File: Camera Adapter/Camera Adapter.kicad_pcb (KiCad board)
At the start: 2 copper layers, 30 x 50 mm, 13 parts, among them J1 Conn_02x15_Top_Bottom, J2 634108150321, J3 Conn_01x02, J4 Conn_01x03, J5 Conn_02x15_Top_Bottom, J6 634108150321, U1 MC33269D-3.3G

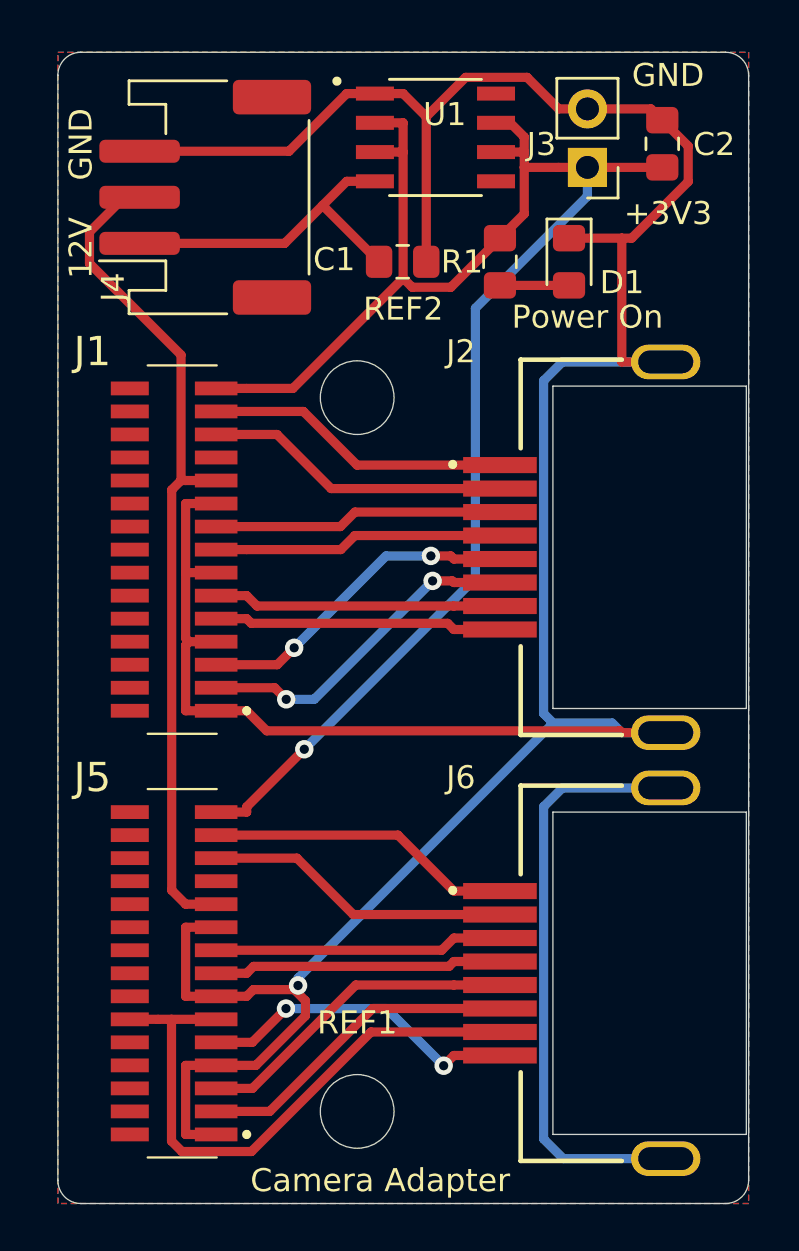
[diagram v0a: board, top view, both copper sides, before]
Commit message: Change to different ZIF connector
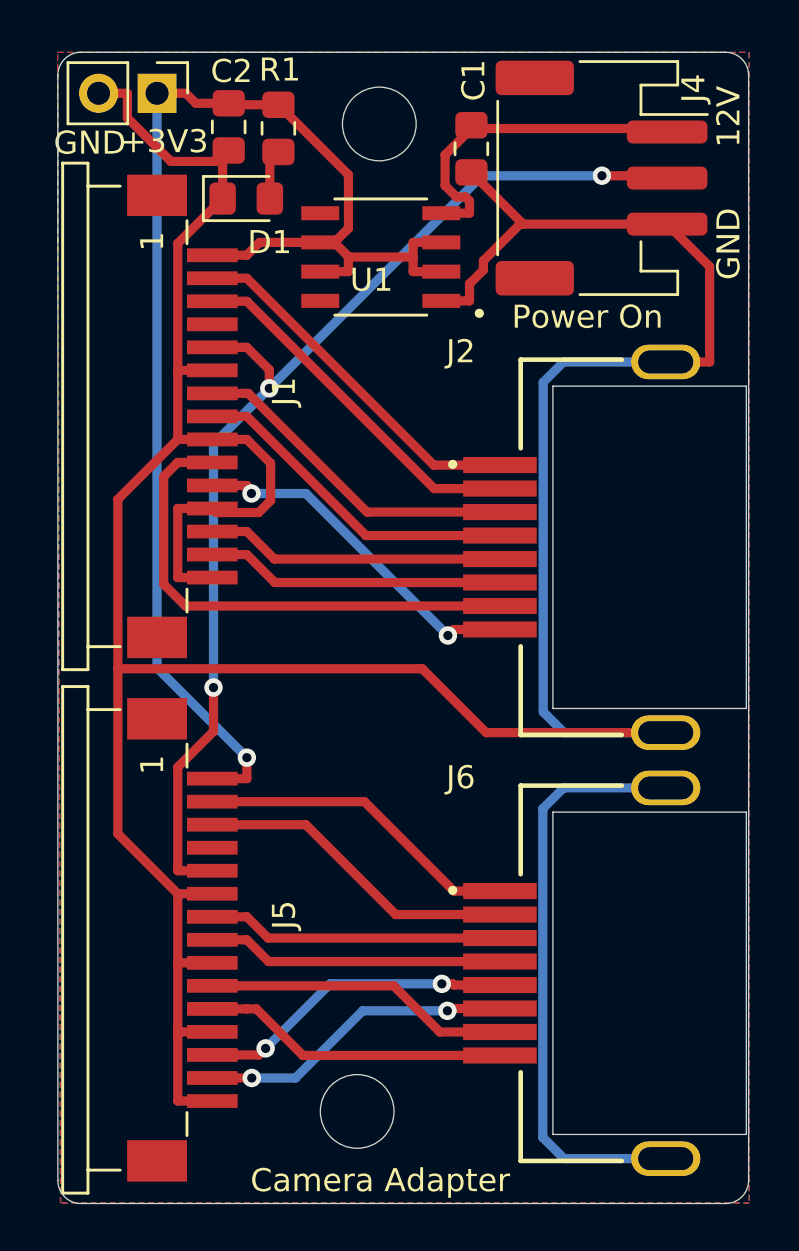
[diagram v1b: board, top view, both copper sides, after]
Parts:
- J1, J5: value Conn_02x15_Top_Bottom -> 68611514122; footprint digikey-footprints:117342485 -> digikey-footprints:68611514122
- moved J3 19.0 mm to (51.3, 29.8), turned to 270 degrees
- moved C2 18.8 mm to (54.4, 31.2), turned to 270 degrees
- moved J4 17.2 mm to (70.6, 33.5), turned to 270 degrees
- moved D1 14.3 mm to (55.2, 34.4), turned to 0 degrees
- moved REF2 11.9 mm to (61.0, 31.1)
- moved R1 11.2 mm to (56.6, 31.3)
- moved J1 6.34 mm to (51.3, 43.8)
- moved C1 5.74 mm to (65.0, 32.2), turned to 270 degrees
- moved U1 5.71 mm to (61.0, 36.9), turned to 180 degrees
- moved J5 2.97 mm to (51.3, 66.5)
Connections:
- J1 pad 1: GND -> +3V3
- J1 pad 10: GND -> CAMERA0DP1
- J1 pad 11: CAMERAGPIO -> CAMERA0DN1
- J1 pad 12: Net-(J1-Pad12) -> GND
- J1 pad 13: CAMERA0SCL -> CAMERA0DP0
- J1 pad 14: CAMERA0SDA -> CAMERA0DN0
- J1 pad 15: +3V3 -> GND
- J1 pad 2: CAMERA0DN0 -> CAMERA0SDA
- J1 pad 3: CAMERA0DP0 -> CAMERA0SCL
- J1 pad 4: GND -> Net-(J1-Pad4)
- J1 pad 5: CAMERA0DN1 -> CAMERAGPIO
- J1 pad 6: CAMERA0DP1 -> GND
- J1 pad 7: GND -> CAMERA0CP
- J1 pad 9: CAMERA0CP -> GND
- J5 pad 1: GND -> +3V3
- J5 pad 10: GND -> CAMERA1DP1
- J5 pad 11: CAMERAGPIO -> CAMERA1DN1
- J5 pad 12: Net-(J5-Pad12) -> GND
- J5 pad 13: CAMERA1SCL -> CAMERA1DP0
- J5 pad 14: CAMERA1SDA -> CAMERA1DN0
- J5 pad 15: +3V3 -> GND
- J5 pad 2: CAMERA1DN0 -> CAMERA1SDA
- J5 pad 3: CAMERA1DP0 -> CAMERA1SCL
- J5 pad 4: GND -> Net-(J5-Pad4)
- J5 pad 5: CAMERA1DN1 -> CAMERAGPIO
- J5 pad 6: CAMERA1DP1 -> GND
- J5 pad 7: GND -> CAMERA1CP
- J5 pad 9: CAMERA1CP -> GND
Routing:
- net +3V3: track 73.5 -> 60.7 mm
- net CAMERA1DP1: track 25.6 -> 13.3 mm
- net CAMERAGPIO: track 36.9 -> 48.9 mm, vias 0 -> 3
- net CAMERA0DP1: track 12.5 -> 22.0 mm
- net CAMERA0DN1: track 12.5 -> 15.4 mm, vias 0 -> 2
- net GND: track 145.6 -> 148.3 mm, vias 1 -> 0
- net CAMERA0SDA: track 13.3 -> 15.9 mm
- net CAMERA0SCL: track 13.3 -> 15.9 mm
- net CAMERA0CN: track 12.6 -> 14.6 mm
- net CAMERA0CP: track 12.6 -> 14.6 mm
- net CAMERA0DN0: track 14.7 -> 13.0 mm, vias 2 -> 0
- net CAMERA0DP0: track 14.3 -> 13.0 mm, vias 2 -> 0
- net Net-(D1-Pad2): track 3.00 -> 2.18 mm
- net CAMERA1DN1: track 14.1 -> 13.3 mm, vias 2 -> 0
- net CAMERA1SDA: track 13.3 -> 14.1 mm
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
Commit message: Updated KiCad files
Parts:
- moved REF2 0.51 mm to (60.5, 31.2)
- moved C1 0.32 mm to (64.6, 32.3)
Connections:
- J6 pad SHIELD1: Net-(J6-PadSHIELD1) -> GND
- J6 pad SHIELD2: Net-(J6-PadSHIELD1) -> GND
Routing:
- net GND: track 148.3 -> 202.5 mm, vias 0 -> 1
- net Net-(J6-PadSHIELD1): track 25.7 -> 0.00 mm
- net CAMERA1DP1: track 13.3 -> 30.8 mm, vias 0 -> 2
- net CAMERA1DN1: track 13.3 -> 21.9 mm
- net +3V3: track 60.7 -> 54.4 mm, vias 1 -> 0
- net CAMERA0DP1: track 22.0 -> 15.8 mm, vias 0 -> 2
- net CAMERAGPIO: track 48.9 -> 49.8 mm
- net CAMERA1DN0: track 13.7 -> 14.1 mm, vias 2 -> 0
- net CAMERA1DP0: vias 2 -> 0
- removed copper zone on B.Cu, net GND
